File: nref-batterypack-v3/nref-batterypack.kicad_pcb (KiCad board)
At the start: 4 copper layers, 75 x 17 mm, 92 parts, among them J0 C1-, J1 C1-, J2 C2+, J3 C3-, J4 C4+, J5 PACK_CONN, J6 BACK_CONN, Q1 BC817, Q2 BC817, Q3 BC817, Q4 BC817, Q5 AO3401A, Q7 AO3401A, Q8 Q_Dual_NMOS_Picostar_CSD87501L, U1 BQ76922

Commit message: battpack v3 snapshot
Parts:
- J5: footprint Connector_JST:JST_SH_SM07B-SRSS-TB_1x07-1MP_P1.00mm_Horizontal -> Connector_JST:JST_SH_BM07B-SRSS-TB_1x07-1MP_P1.00mm_Vertical
- moved R26 9.53 mm to (159.4, 99.2), turned to 0 degrees
- moved Q5 5.10 mm to (156.1, 99.1), turned to -90 degrees
- moved R19 4.75 mm to (156.6, 95.6)
- moved Q8 4.34 mm to (162.1, 99.1), turned to 0 degrees
- moved J5 4.14 mm to (164.6, 93.6), turned to 180 degrees
- moved Q7 4.12 mm to (152.6, 99.1), turned to -90 degrees
- moved D11 3.96 mm to (169.2, 96.8)
- moved R29 3.80 mm to (168.8, 98.0), turned to 180 degrees
- moved R21 3.03 mm to (156.6, 96.6), turned to 180 degrees
- moved D9 2.88 mm to (170.8, 98.0), turned to 0 degrees
- moved D16 2.70 mm to (170.8, 96.8), turned to 180 degrees
- moved R22 2.05 mm to (155.2, 96.2), turned to -90 degrees
- moved R23 1.25 mm to (153.4, 97.9)
- moved R25 1.25 mm to (153.8, 96.4)
- moved R27 1.25 mm to (153.3, 95.0)
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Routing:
- net /VC5: track 38.3 -> 25.1 mm
- net /C3+: track 46.3 -> 34.7 mm
- net /DSG: track 18.5 -> 12.1 mm
- net /LD: track 14.8 -> 10.2 mm
- net /PCHG: track 12.8 -> 8.83 mm
- net /PDSG: track 11.6 -> 7.81 mm
- net /PACK+: track 25.0 -> 21.3 mm
- net Net-(Q8-G1): track 4.16 -> 0.55 mm, vias 2 -> 1
- net /CHG: track 13.7 -> 11.0 mm
- net /SDA: track 0.00 -> 1.32 mm, vias 0 -> 1
- net /SCL: track 0.00 -> 1.32 mm, vias 0 -> 1
- net /ALERT: track 0.00 -> 1.32 mm, vias 0 -> 1
- net /BATplus: track 9.15 -> 10.3 mm
- net GND: vias 39 -> 28

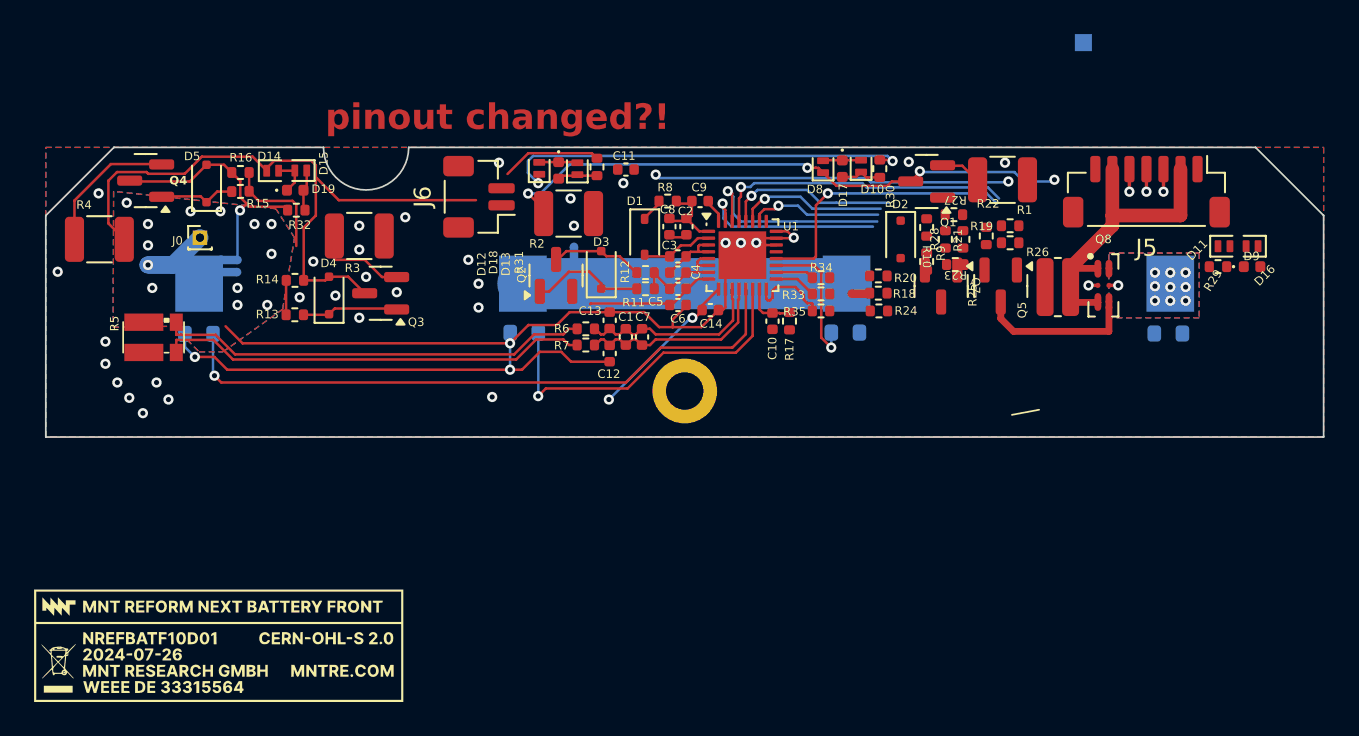
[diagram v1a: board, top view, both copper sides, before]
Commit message: battpack v3 (front) rerouting complete
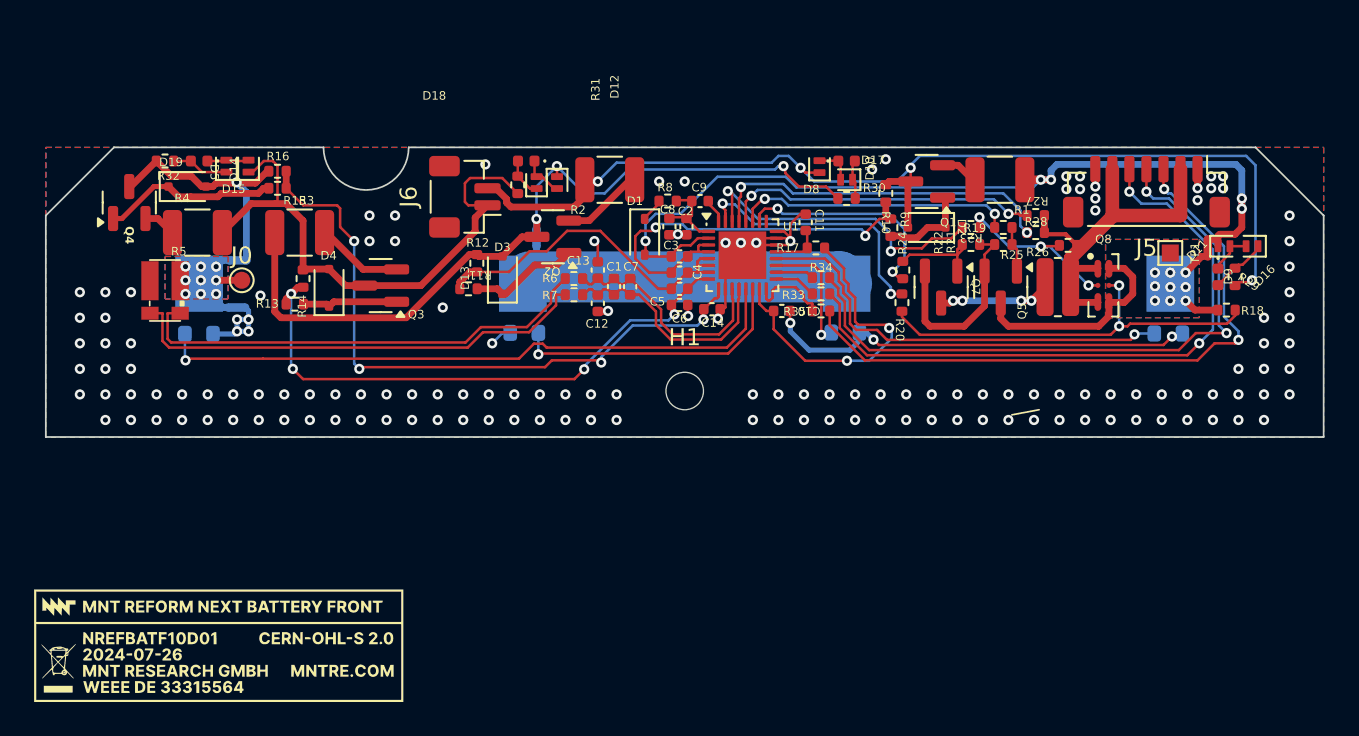
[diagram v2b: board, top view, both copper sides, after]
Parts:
- H1: footprint MountingHole:MountingHole_2.2mm_M2_DIN965_Pad -> MountingHole:MountingHole_2.2mm_M2
- J0: footprint Connector_PinHeader_1.00mm:PinHeader_1x01_P1.00mm_Vertical -> TestPoint:TestPoint_Pad_D1.0mm
- TP1: moved to F.Cu
- moved NT4.0 20.6 mm to (168.2, 96.9), turned to -90 degrees
- moved R18 20.5 mm to (169.3, 100.5)
- moved TP1 13.4 mm to (166.0, 97.2), turned to -90 degrees
- moved C11 11.0 mm to (144.6, 95.4), turned to -90 degrees
- moved R11 10.4 mm to (124.8, 99.3), turned to 0 degrees
- moved R12 9.92 mm to (125.3, 97.8), turned to 90 degrees
- moved R32 8.23 mm to (107.0, 91.8)
- moved R25 6.18 mm to (160.0, 96.8), turned to 0 degrees
- moved D19 5.89 mm to (109.0, 91.8), turned to 180 degrees
- moved D3 5.81 mm to (126.8, 98.5)
- moved R4 5.77 mm to (108.9, 96.0)
- moved R28 5.32 mm to (158.1, 96.0), turned to 0 degrees
- moved R27 4.80 mm to (158.1, 95.0)
- moved R31 4.77 mm to (127.7, 93.2), turned to -90 degrees
- moved R17 4.57 mm to (145.2, 96.9), turned to 0 degrees
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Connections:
- C11 pad 1: GND -> VSS
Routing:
- net /SDA: track 1.32 -> 38.7 mm, vias 1 -> 2
- net /ALERT: track 1.32 -> 38.1 mm, vias 1 -> 2
- net /SCL: track 1.32 -> 37.8 mm, vias 1 -> 2
- net /C3+: track 34.7 -> 63.6 mm
- net /VC5: track 25.1 -> 51.7 mm, vias 2 -> 5
- net /VC1: track 9.71 -> 34.0 mm, vias 0 -> 4
- net VSS: track 71.6 -> 48.1 mm, vias 7 -> 17
- net Net-(Q8-G2): track 0.79 -> 24.1 mm, vias 1 -> 2
- net /VC0: track 15.9 -> 38.7 mm, vias 2 -> 4
- net /VC4: track 3.74 -> 24.8 mm, vias 0 -> 2
- net Net-(D12-K): track 30.0 -> 46.9 mm, vias 2 -> 3
- net +1V8: track 3.07 -> 19.1 mm, vias 0 -> 2
- net /VC2: track 7.00 -> 20.2 mm
- net Net-(Q5-S): track 0.00 -> 11.8 mm
- net /C1+: track 44.4 -> 33.0 mm
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- added copper zone on In1.Cu, net VSS
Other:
- board text removed: "1"
- board text removed: "2"
- board text removed: "3"
- board text removed: "4"
- board text removed: "pinout changed?!"

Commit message: battpack v3 (front): routing polishing, 3d models
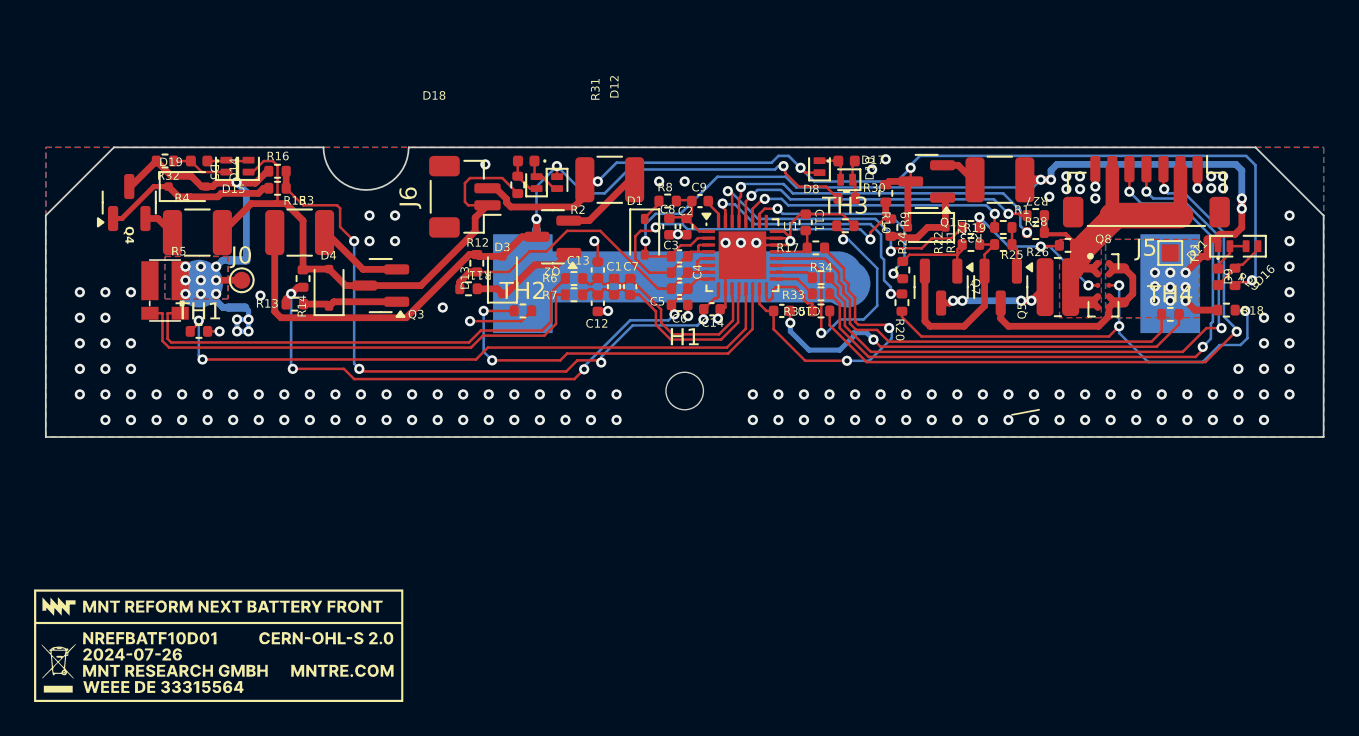
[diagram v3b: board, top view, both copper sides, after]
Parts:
- J1, J3: footprint Automated:S713145R -> footprints:S70332002045R
- J2, J4: footprint Automated:S713145R -> footprints:S174146R
- TH1, TH2, TH3, TH4: footprint Resistor_SMD:R_0603_1608Metric -> Resistor_SMD:R_0402_1005Metric; moved to F.Cu
- moved TH3 6.27 mm to (146.9, 95.6)
- moved TH2 1.29 mm to (128.0, 100.6), turned to 0 degrees
- moved TH4 1.13 mm to (166.0, 100.8)
- moved TH1 0.15 mm to (109.0, 101.8)
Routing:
- net /TS3: track 7.12 -> 16.2 mm, vias 1 -> 2
- net /TS2: track 16.8 -> 23.3 mm, vias 1 -> 2
- net VSS: track 48.1 -> 53.6 mm
- net Net-(Q8-G2): track 24.1 -> 28.3 mm, vias 2 -> 3
- net /TS4: track 25.7 -> 27.3 mm, vias 1 -> 0
- net /SCL: track 37.8 -> 38.6 mm
- net /Cell23: track 20.7 -> 20.1 mm
- net /PACK+: track 24.5 -> 25.2 mm
- net /CSENSE_N: track 27.8 -> 28.4 mm
- net /CSENSE_P: track 27.6 -> 28.2 mm
- net /TS1: track 37.7 -> 38.2 mm, vias 1 -> 2
- net GND: vias 132 -> 131
- added copper zone on F.Cu, net /PACK+

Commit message: battpack v3 (front) silkscreen
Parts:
- G***: moved to B.Cu
- moved G*** 16.1 mm to (111.3, 104.2), turned to 180 degrees
- turned D12 to 90 degrees
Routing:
- net Net-(D12-K): track 46.9 -> 49.2 mm
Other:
- board text added: "+"
- board text added: "-"

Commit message: batterypack v3 front+back pcbs polished for ordering
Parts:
- J6: footprint Connector_JST:JST_SH_BM02B-SRSS-TB_1x02-1MP_P1.00mm_Vertical -> Connector_JST:JST_SH_SM02B-SRSS-TB_1x02-1MP_P1.00mm_Horizontal
- moved R3 1.10 mm to (113.8, 96.0)
- moved NT3 0.85 mm to (128.8, 95.5), turned to 0 degrees
- moved J6 0.71 mm to (123.9, 93.8), turned to -90 degrees
- moved G*** 0.10 mm to (111.3, 104.3)
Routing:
- net /Cell23: track 20.1 -> 24.2 mm
- net /C3+: track 63.6 -> 61.2 mm
- net Net-(Q8-G1): track 10.3 -> 8.93 mm
- net /VC0: track 38.9 -> 37.7 mm
- net /bqPACK: track 20.6 -> 21.8 mm
- net Net-(Q3-C): track 5.13 -> 6.23 mm
- net /C1+: track 33.0 -> 32.0 mm
- net Net-(Q7-G): track 5.77 -> 5.07 mm
- net GND: vias 131 -> 141
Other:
- outline, holes or cut-outs redrawn
- board text added: "AL"
- board text added: "BAT+"
- board text added: "GND"
- board text added: "P+"
- board text added: "SC"
- board text added: "SD"
- board text added: "–"
- board text removed: "-"

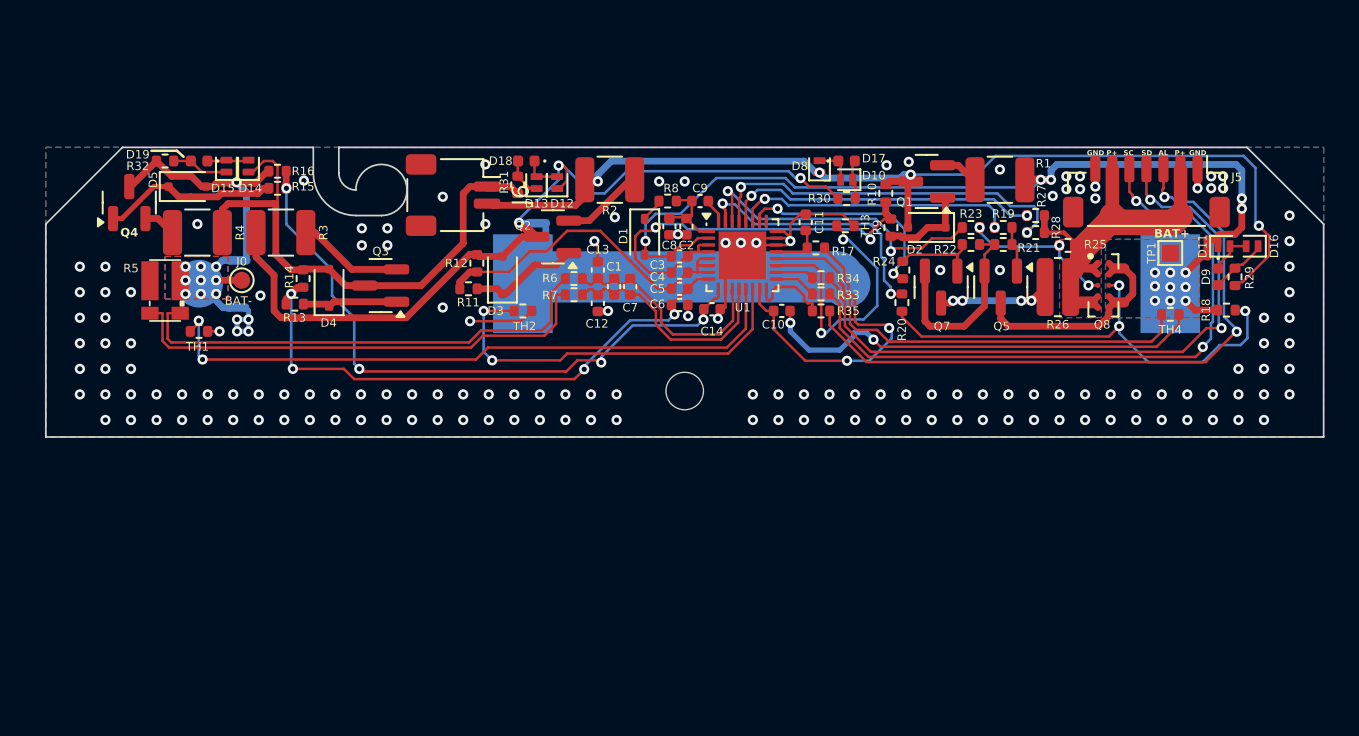
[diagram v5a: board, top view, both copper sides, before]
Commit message: batterypack back/front: polishing for production
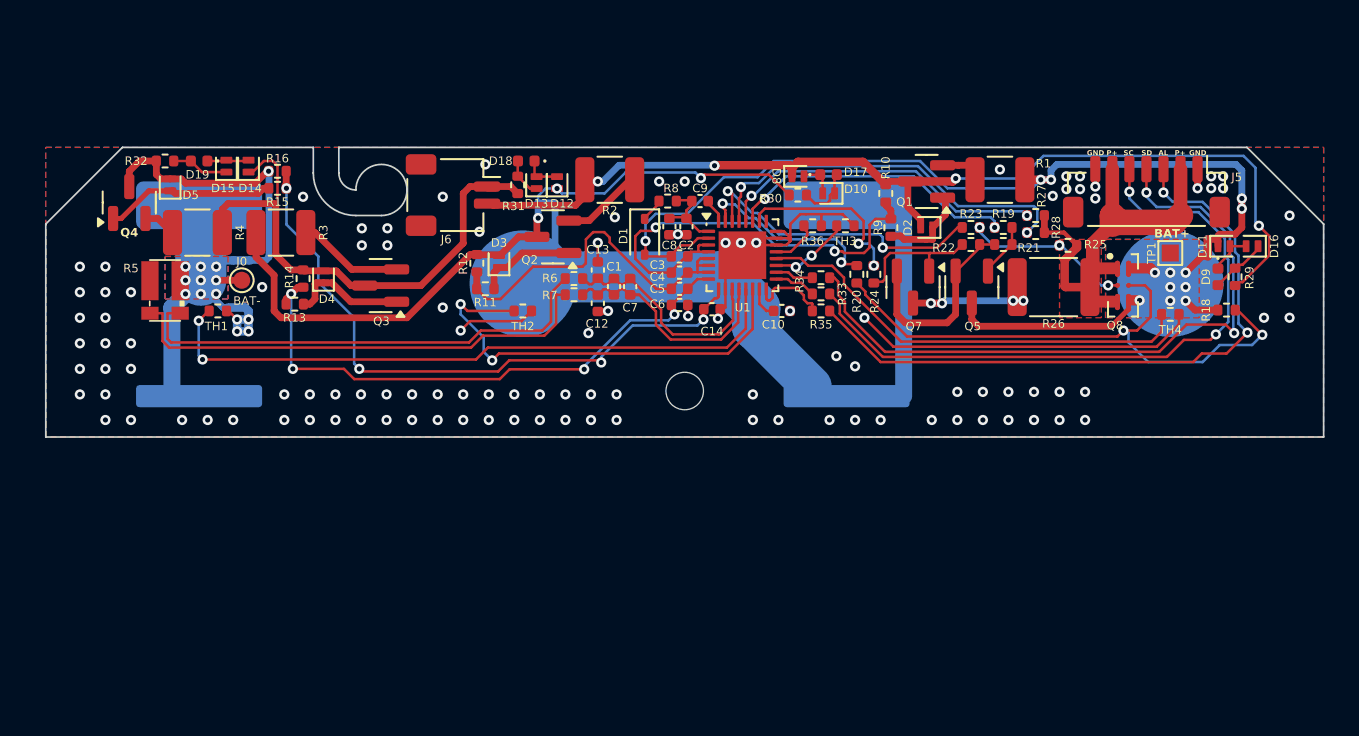
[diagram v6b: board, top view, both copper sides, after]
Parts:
- removed C11: 100nF, Capacitor_SMD:C_0402_1005Metric
- removed R17: 100, Resistor_SMD:R_0402_1005Metric
- added R36: 10k, Resistor_SMD:R_0402_1005Metric, F.Cu at (145.0, 95.6)
- C10: value 2.2uF -> 2.2uF/25V
- D2, D3, D4, D5: footprint Diode_SMD:D_SOD-323F -> Diode_SMD:D_SOD-882
- J1, J3: footprint footprints:S70332002045R -> footprints:MYOUNG_MY-FJ-115
- J2, J4: footprint footprints:S174146R -> footprints:Mill-Max_2036-X-57
- R26: footprint Resistor_SMD:R_0612_1632Metric -> Resistor_SMD:R_1812_4532Metric
- moved G*** 54.7 mm to (165.9, 105.0)
- moved R20 3.13 mm to (147.6, 98.5)
- moved R30 2.87 mm to (144.1, 93.8)
- moved R24 1.72 mm to (148.6, 98.5), turned to -90 degrees
- moved Q5 1.70 mm to (154.3, 99.2)
- moved Q7 1.65 mm to (150.9, 99.2)
- moved TH1 1.63 mm to (110.1, 100.6)
- moved D8 1.38 mm to (144.2, 92.7), turned to 0 degrees
- moved D17 1.33 mm to (145.9, 92.6)
- moved D10 1.32 mm to (145.9, 93.7)
- moved NT3 1.26 mm to (129.4, 94.3)
- moved Q8 1.15 mm to (163.2, 99.1)
- moved D5 1.00 mm to (107.3, 93.2), turned to 90 degrees
- moved J1 1.00 mm to (109.0, 100.0), turned to 0 degrees
- moved J3 1.00 mm to (147.0, 100.0), turned to 0 degrees
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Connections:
- U1 pad 21: /~{RST} -> /RST
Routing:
- net +1V8: track 19.1 -> 1.87 mm, vias 2 -> 0
- net /Cell23: track 24.2 -> 37.2 mm
- net /TS3: track 16.2 -> 4.81 mm
- net /BAT-: track 6.12 -> 17.2 mm
- net Net-(D12-K): track 49.3 -> 41.3 mm
- net Net-(Q8-G2): track 28.3 -> 34.2 mm, vias 3 -> 2
- net VSS: track 53.6 -> 48.8 mm, vias 17 -> 15
- net /CHG: track 15.5 -> 11.3 mm
- net /~{RST}: track 2.97 -> 0.00 mm
- net Net-(Q7-G): track 5.07 -> 7.94 mm
- net /PDSG: track 13.1 -> 10.4 mm
- net /RST: track 0.00 -> 2.53 mm
- net /TS2: track 23.3 -> 25.8 mm
- net Net-(D5-A): track 14.7 -> 16.9 mm
- net /SDA: track 38.8 -> 40.5 mm
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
